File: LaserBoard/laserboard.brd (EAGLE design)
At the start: 76.2 x 76.2 mm, 22 parts, among them Q1 BSS138

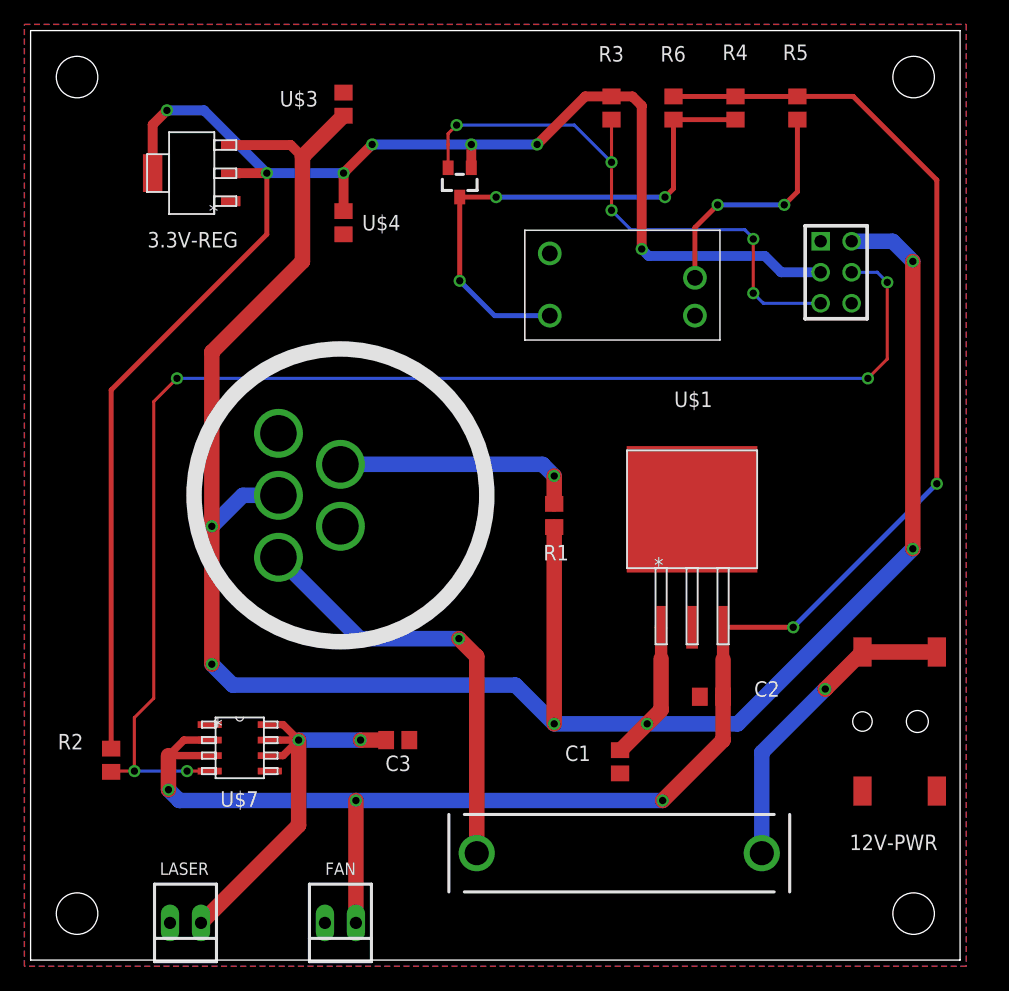
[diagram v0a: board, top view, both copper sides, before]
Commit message: Updates to Laser and Power Board
Updated emergency shutoff button footprint, led button voltage changed
to 5v, and switched level shifter to 74LVC1T45.
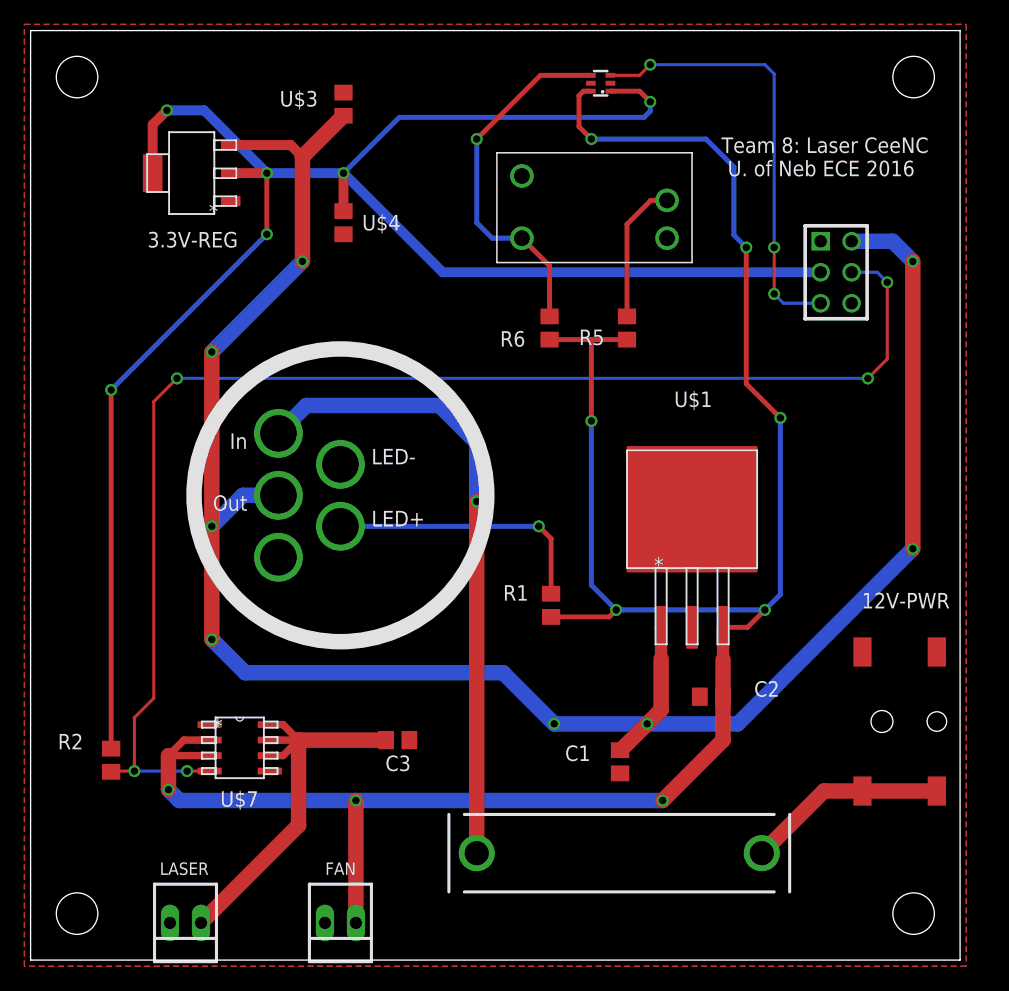
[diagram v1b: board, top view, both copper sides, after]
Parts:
- removed Q1: BSS138, m-pad-2.1:SOT23
- removed R3, R4: 10K, rcl:R0805
- added U$2: 74LVC1T45, ChristiansCustom:SOT363
- R1: value 510Ω 1/2W -> 155
- moved R5 22.8 mm to (48.9, 51.8), turned to 90 degrees
- moved R6 20.7 mm to (42.5, 51.8), turned to 90 degrees
- moved R1 7.37 mm to (42.7, 29.1)
- moved U$9 6.75 mm to (46.2, 59.2)
- turned 12V-PWR to 180 degrees
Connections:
- net +12V: no longer R1.2
- net +3V3: now also U$2.1; no longer Q1.1, R3.2
- net +5V: now also R1.2, U$2.6; no longer R4.2
- net GND: now also U$2.2, U$2.5
- net N$5: now also U$2.4; no longer Q1.3, R4.1
- net TILT: now also U$2.3; no longer Q1.2, R3.1
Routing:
- net +5V: track 149.0 -> 184.5 mm, vias 5 -> 9
- net +3V3: track 137.3 -> 154.9 mm, vias 7 -> 6
- net +12V: track 184.6 -> 167.3 mm, vias 6 -> 8
- net N$3: track 35.8 -> 52.1 mm
- net N$5: track 44.0 -> 30.0 mm, vias 3 -> 1
- net TILT: track 48.1 -> 36.3 mm, vias 5 -> 3
- net N$2: track 26.0 -> 16.5 mm, vias 1 -> 0
- net N$7: track 19.6 -> 11.7 mm, vias 2 -> 0
- net N$1: track 20.2 -> 22.2 mm
- net LSR_PWR: vias 2 -> 0
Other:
- board text added: "Team 8: Laser CeeNC U. of Neb ECE 2016"

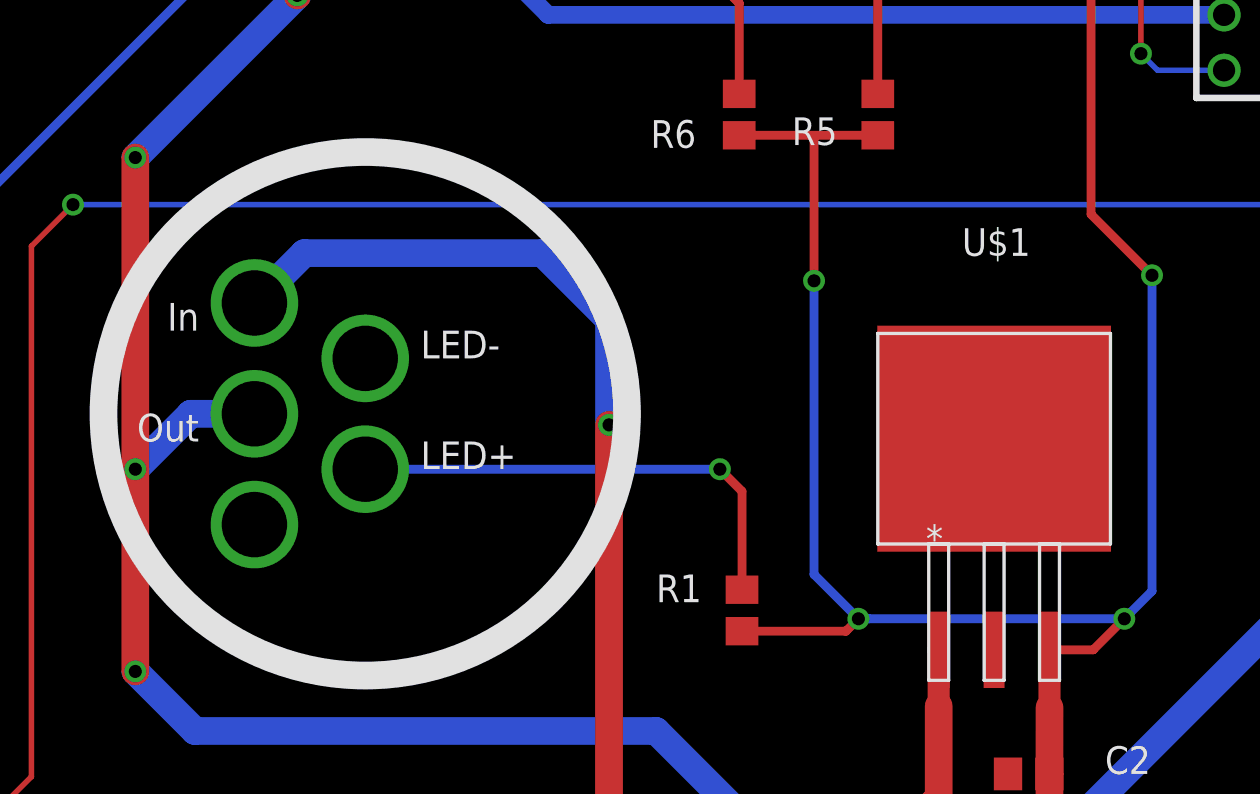
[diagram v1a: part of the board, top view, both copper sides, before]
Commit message: Final Revisions to PCBs and Schematics
Final revisions made to the PCBs and schematics. This is the version
which will be sent out to the board house for round two.
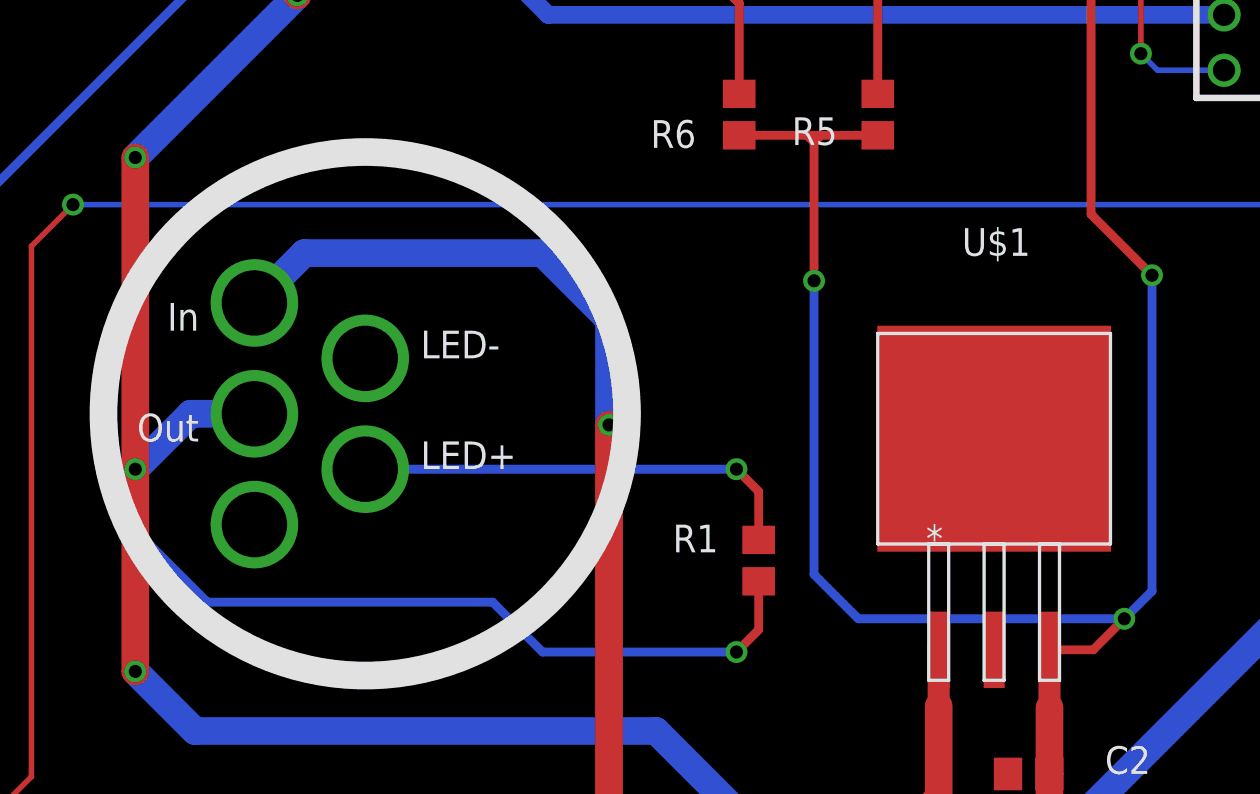
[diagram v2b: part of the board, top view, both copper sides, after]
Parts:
- R1: value 155 -> 510
- moved R1 2.41 mm to (43.4, 31.4)
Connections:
- net +12V: now also R1.2
- net +5V: no longer R1.2
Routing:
- net +12V: track 167.3 -> 203.6 mm, vias 8 -> 9
- net +5V: track 184.5 -> 179.7 mm, vias 9 -> 8
- net N$1: track 22.2 -> 20.7 mm
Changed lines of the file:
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@@
 <attribute name="NAME" x="75.358" y="30.1" size="1.27" layer="25" rot="R180"/>
 </element>
-<element name="R1" library="rcl" package="R0805" value="155" x="42.672" y="29.083" smashed="yes" rot="R270">
-<attribute name="NAME" x="38.735" y="29.464" size="1.27" layer="25"/>
-<attribute name="VALUE" x="38.227" y="27.559" size="1.27" layer="27"/>
+<element name="R1" library="rcl" package="R0805" value="510" x="43.434" y="31.369" smashed="yes" rot="R270">
+<attribute name="NAME" x="39.497" y="31.75" size="1.27" layer="25"/>
+<attribute name="VALUE" x="38.989" y="29.845" size="1.27" layer="27"/>
 </element>
 <element name="R2" library="rcl" package="R0805" value="10K" x="6.604" y="16.383" smashed="yes" rot="R90">
@@
 <via x="60.198" y="28.702" extent="1-16" drill="0.6"/>
 <via x="45.974" y="44.196" extent="1-16" drill="0.6"/>
-<wire x1="45.974" y1="44.196" x2="45.974" y2="50.866" width="0.4064" layer="1"/>
+<wire x1="45.974" y1="44.196" x2="45.974" y2="50.546" width="0.4064" layer="1"/>
+<wire x1="45.974" y1="50.546" x2="45.974" y2="50.866" width="0.4064" layer="1"/>
 <wire x1="45.936" y1="71.232" x2="45.324" y2="71.232" width="0.4064" layer="1"/>
 <wire x1="45.324" y1="71.232" x2="44.958" y2="70.866" width="0.4064" layer="1"/>
@@
 <wire x1="48.006" y1="28.702" x2="45.974" y2="30.734" width="0.4064" layer="16"/>
 <wire x1="45.974" y1="30.734" x2="45.974" y2="44.196" width="0.4064" layer="16"/>
-<contactref element="R1" pad="2"/>
-<wire x1="42.672" y1="28.133" x2="47.437" y2="28.133" width="0.4064" layer="1"/>
-<wire x1="48.514" y1="28.702" x2="60.198" y2="28.702" width="0.4064" layer="16"/>
-<wire x1="47.437" y1="28.133" x2="48.006" y2="28.702" width="0.4064" layer="1"/>
-<via x="48.006" y="28.702" extent="1-16" drill="0.6"/>
-<wire x1="48.006" y1="28.702" x2="48.514" y2="28.702" width="0.4064" layer="16"/>
+<wire x1="48.006" y1="28.702" x2="60.198" y2="28.702" width="0.4064" layer="16"/>
+<wire x1="45.974" y1="50.546" x2="46.228" y2="50.8" width="0.4064" layer="1"/>
+<wire x1="45.974" y1="50.546" x2="45.72" y2="50.8" width="0.4064" layer="1"/>
 </signal>
 <signal name="+12V">
@@
 <via x="14.859" y="49.8475" extent="1-16" drill="0.6"/>
 <via x="22.2885" y="57.277" extent="1-16" drill="0.6"/>
+<contactref element="R1" pad="2"/>
+<wire x1="43.434" y1="30.419" x2="43.434" y2="28.194" width="0.4064" layer="1"/>
+<wire x1="43.434" y1="28.194" x2="42.418" y2="27.178" width="0.4064" layer="1"/>
+<via x="42.418" y="27.178" extent="1-16" drill="0.6"/>
+<wire x1="42.418" y1="27.178" x2="33.528" y2="27.178" width="0.4064" layer="16"/>
+<wire x1="33.528" y1="27.178" x2="31.242" y2="29.464" width="0.4064" layer="16"/>
+<wire x1="31.242" y1="29.464" x2="18.161" y2="29.464" width="0.4064" layer="16"/>
+<wire x1="18.161" y1="29.464" x2="14.859" y2="32.766" width="0.4064" layer="16"/>
+<wire x1="14.859" y1="32.766" x2="14.859" y2="35.56" width="0.4064" layer="16"/>
 </signal>
 <signal name="N$2">
@@
 <contactref element="R1" pad="1"/>
 <contactref element="U$5" pad="+"/>
-<wire x1="42.672" y1="30.033" x2="42.672" y2="34.544" width="0.4064" layer="1"/>
-<wire x1="42.672" y1="34.544" x2="41.656" y2="35.56" width="0.4064" layer="1"/>
-<via x="41.656" y="35.56" extent="1-16" drill="0.6"/>
-<wire x1="41.656" y1="35.56" x2="25.4" y2="35.56" width="0.4064" layer="16"/>
+<wire x1="43.434" y1="32.319" x2="43.434" y2="34.544" width="0.4064" layer="1"/>
+<wire x1="43.434" y1="34.544" x2="42.418" y2="35.56" width="0.4064" layer="1"/>
+<via x="42.418" y="35.56" extent="1-16" drill="0.6"/>
+<wire x1="42.418" y1="35.56" x2="25.4" y2="35.56" width="0.4064" layer="16"/>
 </signal>
 </signals>
